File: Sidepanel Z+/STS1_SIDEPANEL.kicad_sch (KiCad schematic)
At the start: 3 parts, among them J1 Conn_02x04_Odd_Even, J2 Conn_02x02_Odd_Even

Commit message: Next fix
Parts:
- added J3: Conn_02x02_Odd_Even, STS_Connector:M808280442, symbol Connector_Generic:Conn_02x02_Odd_Even
- added TH1: Thermistor_NTC, Resistor_SMD:R_0805_2012Metric_Pad1.20x1.40mm_HandSolder, symbol Device:Thermistor_NTC
- Outline1: footprint USER_OUTLINE:OUTLINE_SidepanelY+ -> USER_OUTLINE:OUTLINE_SidepanelZ+
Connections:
- net GND: now also TH1.2
- net TEMP+: now also TH1.1
- new net AntennaDeployment/ANT_DEPLOY+: J3.1 (Pin_1), J3.2 (Pin_2)
- new net AntennaDeployment/ANT_DEPLOY-: J3.3 (Pin_3), J3.4 (Pin_4)
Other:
- added sheet AntennaDeployment (AntennaDeployment.kicad_sch)
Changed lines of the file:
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@@
 (kicad_sch (version 20211123) (generator eeschema)
   (paper "A4")
+  (junction (at 134.62 74.93) (diameter 0) (color 0 0 0 0)
+  )
+  (junction (at 134.62 72.39) (diameter 0) (color 0 0 0 0)
+  )
+  (wire (pts (xy 121.92 74.93) (xy 134.62 74.93))
+    (stroke (width 0) (type default) (color 0 0 0 0))
+  )
   (wire (pts (xy 26.67 67.31) (xy 34.29 67.31))
     (stroke (width 0) (type default) (color 0 0 0 0))
   )
+  (wire (pts (xy 138.43 39.37) (xy 152.4 39.37))
+    (stroke (width 0) (type default) (color 0 0 0 0))
+  )
   (wire (pts (xy 54.61 74.93) (xy 46.99 74.93))
     (stroke (width 0) (type default) (color 0 0 0 0))
@@
     (stroke (width 0) (type default) (color 0 0 0 0))
   )
+  (wire (pts (xy 134.62 35.56) (xy 152.4 35.56))
+    (stroke (width 0) (type default) (color 0 0 0 0))
+  )
   (wire (pts (xy 72.39 39.37) (xy 82.55 39.37))
     (stroke (width 0) (type default) (color 0 0 0 0))
@@
     (stroke (width 0) (type default) (color 0 0 0 0))
   )
+  (wire (pts (xy 30.48 93.345) (xy 30.48 97.155))
+    (stroke (width 0) (type default) (color 0 0 0 0))
+  )
+  (wire (pts (xy 138.43 74.93) (xy 138.43 39.37))
+    (stroke (width 0) (type default) (color 0 0 0 0))
+  )
+  (wire (pts (xy 134.62 74.93) (xy 138.43 74.93))
+    (stroke (width 0) (type default) (color 0 0 0 0))
+  )
   (wire (pts (xy 72.39 31.75) (xy 82.55 31.75))
     (stroke (width 0) (type default) (color 0 0 0 0))
@@
     (stroke (width 0) (type default) (color 0 0 0 0))
   )
+  (wire (pts (xy 134.62 72.39) (xy 134.62 35.56))
+    (stroke (width 0) (type default) (color 0 0 0 0))
+  )
   (wire (pts (xy 92.71 72.39) (xy 100.33 72.39))
     (stroke (width 0) (type default) (color 0 0 0 0))
   )
+  (wire (pts (xy 121.92 72.39) (xy 134.62 72.39))
+    (stroke (width 0) (type default) (color 0 0 0 0))
+  )
   (wire (pts (xy 72.39 41.91) (xy 82.55 41.91))
     (stroke (width 0) (type default) (color 0 0 0 0))
   )
+  (wire (pts (xy 30.48 104.775) (xy 30.48 107.95))
+    (stroke (width 0) (type default) (color 0 0 0 0))
+  )
   (wire (pts (xy 46.99 69.85) (xy 58.42 69.85))
     (stroke (width 0) (type default) (color 0 0 0 0))
@@
     (stroke (width 0) (type default) (color 0 0 0 0))
   )
+  (wire (pts (xy 30.48 93.345) (xy 37.465 93.345))
+    (stroke (width 0) (type default) (color 0 0 0 0))
+  )
   (wire (pts (xy 96.52 29.21) (xy 104.14 29.21))
     (stroke (width 0) (type default) (color 0 0 0 0))
@@
   )
   (label "SC1_V+" (at 82.55 29.21 180)
+    (effects (font (size 1.27 1.27)) (justify right bottom))
+  )
+  (label "TEMP+" (at 37.465 93.345 180)
     (effects (font (size 1.27 1.27)) (justify right bottom))
   )
@@
       (effects (font (size 1.27 1.27)) (justify left))
     )
-    (property "Footprint" "USER_OUTLINE:OUTLINE_SidepanelY+" (id 2) (at 22.86 22.86 0)
+    (property "Footprint" "USER_OUTLINE:OUTLINE_SidepanelZ+" (id 2) (at 22.86 22.86 0)
       (effects (font (size 1.27 1.27)) hide)
     )
@@
       (effects (font (size 1.27 1.27)) hide)
     )
+  )
+  (symbol (lib_id "power:GND") (at 30.48 107.95 0) (unit 1)
+    (in_bom yes) (on_board yes) (fields_autoplaced)
+    (property "Reference" "#PWR0113" (id 0) (at 30.48 114.3 0)
+      (effects (font (size 1.27 1.27)) hide)
+    )
+    (property "Value" "GND" (id 1) (at 30.48 113.03 0))
+    (property "Footprint" "" (id 2) (at 30.48 107.95 0)
+      (effects (font (size 1.27 1.27)) hide)
+    )
+    (property "Datasheet" "" (id 3) (at 30.48 107.95 0)
+      (effects (font (size 1.27 1.27)) hide)
+    )
+    (pin "1")
   )
   (symbol (lib_id "Connector_Generic:Conn_02x04_Odd_Even") (at 39.37 69.85 0) (unit 1)
@@
     (pin "4")
   )
+  (symbol (lib_id "Device:Thermistor_NTC") (at 30.48 100.965 0) (unit 1)
+    (in_bom yes) (on_board yes) (fields_autoplaced)
+    (property "Reference" "TH1" (id 0) (at 33.02 100.0124 0)
+      (effects (font (size 1.27 1.27)) (justify left))
+    )
+    (property "Value" "Thermistor_NTC" (id 1) (at 33.02 102.5524 0)
+      (effects (font (size 1.27 1.27)) (justify left))
+    )
+    (property "Footprint" "Resistor_SMD:R_0805_2012Metric_Pad1.20x1.40mm_HandSolder" (id 2) (at 30.48 99.695 0)
+      (effects (font (size 1.27 1.27)) hide)
+    )
+    (property "Datasheet" "~" (id 3) (at 30.48 99.695 0)
+      (effects (font (size 1.27 1.27)) hide)
+    )
+    (pin "1")
+    (pin "2")
+  )
+  (symbol (lib_id "Connector_Generic:Conn_02x02_Odd_Even") (at 127 72.39 0) (unit 1)
+    (in_bom yes) (on_board yes) (fields_autoplaced)
+    (property "Reference" "J3" (id 0) (at 128.27 67.4202 0))
+    (property "Value" "Conn_02x02_Odd_Even" (id 1) (at 128.27 69.9571 0))
+    (property "Footprint" "STS_Connector:M808280442" (id 2) (at 127 72.39 0)
+      (effects (font (size 1.27 1.27)) hide)
+    )
+    (property "Datasheet" "~" (id 3) (at 127 72.39 0)
+      (effects (font (size 1.27 1.27)) hide)
+    )
+    (pin "1")
+    (pin "2")
+    (pin "3")
+    (pin "4")
+  )
   (symbol (lib_id "power:GND") (at 101.6 76.2 0) (unit 1)
     (in_bom yes) (on_board yes) (fields_autoplaced)
@@
     )
     (pin "1")
+  )
+  (sheet (at 152.4 26.67) (size 21.59 15.24) (fields_autoplaced)
+    (stroke (width 0.1524) (type solid) (color 0 0 0 0))
+    (fill (color 0 0 0 0.0000))
+    (property "Sheet name" "AntennaDeployment" (id 0) (at 152.4 25.9584 0)
+      (effects (font (size 1.27 1.27)) (justify left bottom))
+    )
+    (property "Sheet file" "AntennaDeployment.kicad_sch" (id 1) (at 152.4 42.4946 0)
+      (effects (font (size 1.27 1.27)) (justify left top))
+    )
+    (pin "ANT_DEPLOY+" input (at 152.4 35.56 180)
+      (effects (font (size 1.27 1.27)) (justify left))
+    )
+    (pin "ANT_DEPLOY-" input (at 152.4 39.37 180)
+      (effects (font (size 1.27 1.27)) (justify left))
+    )
   )
   (sheet (at 50.8 26.67) (size 21.59 20.32) (fields_autoplaced)
@@
     (path "/9d03bb93-a9aa-424f-bd25-022f173efd1d" (page "3"))
     (path "/4f87559b-6bba-4ff6-97a7-dad9a308db2d" (page "4"))
+    (path "/13fd01c2-9c13-4b4c-bd8b-0bea989ca11e" (page "4"))
   )
   (symbol_instances
@@
       (reference "#PWR0112") (unit 1) (value "GND") (footprint "")
     )
+    (path "/7b859b76-0528-49b2-a54e-fd6560111b42"
+      (reference "#PWR0113") (unit 1) (value "GND") (footprint "")
+    )
     (path "/9d03bb93-a9aa-424f-bd25-022f173efd1d/744ba6a5-8f97-44b6-b33c-eda609bf7e9f"
       (reference "C1") (unit 1) (value "1u") (footprint "Capacitor_SMD:C_0603_1608Metric")
@@
     )
     (path "/4f87559b-6bba-4ff6-97a7-dad9a308db2d/65c76957-ccfc-4d5b-b7d9-2ee7c354f524"
-      (reference "DOUT2") (unit 1) (value "SMM4F5.0") (footprint "Diode_SMD:D_0603_1608Metric")
+      (reference "DOUT2") (unit 1) (value "SMM4F5.0") (footprint "LED_SMD:LED_0603_1608Metric")
     )
     (path "/9d03bb93-a9aa-424f-bd25-022f173efd1d/d9839939-8918-48f3-b4b2-d753b1d9a645"
@@
       (reference "J2") (unit 1) (value "Conn_02x02_Odd_Even") (footprint "STS_Connector:M808280442")
     )
+    (path "/bc26867e-2044-46bb-8920-dfb46ce37aad"
+      (reference "J3") (unit 1) (value "Conn_02x02_Odd_Even") (footprint "STS_Connector:M808280442")
+    )
     (path "/4f87559b-6bba-4ff6-97a7-dad9a308db2d/bfe4e68f-4cef-4b31-adff-8df094bc3870"
-      (reference "L_IN1") (unit 1) (value "10u") (footprint "Inductor_SMD:L_0603_1608Metric")
+      (reference "L_IN1") (unit 1) (value "10u") (footprint "Inductor_SMD:L_0805_2012Metric")
     )
     (path "/4f87559b-6bba-4ff6-97a7-dad9a308db2d/06a966cd-4913-436b-a217-7ac14ca6801e"
-      (reference "L_IN2") (unit 1) (value "10u") (footprint "Inductor_SMD:L_0603_1608Metric")
+      (reference "L_IN2") (unit 1) (value "10u") (footprint "Inductor_SMD:L_0805_2012Metric")
     )
     (path "/4f87559b-6bba-4ff6-97a7-dad9a308db2d/679b2e27-da22-4f13-a86e-25be83598a10"
@@
     )
     (path "/6503b427-07c6-4391-8fa6-4757fb4daa6c"
-      (reference "Outline1") (unit 1) (value "OUTLINE_Sidepanel") (footprint "USER_OUTLINE:OUTLINE_SidepanelY+")
+      (reference "Outline1") (unit 1) (value "OUTLINE_Sidepanel") (footprint "USER_OUTLINE:OUTLINE_SidepanelZ+")
     )
     (path "/4f87559b-6bba-4ff6-97a7-dad9a308db2d/548d9577-1c12-4167-8fdd-bb768e95bfba"
@@
       (reference "R32") (unit 1) (value "1k") (footprint "Resistor_SMD:R_0603_1608Metric")
     )
+    (path "/13fd01c2-9c13-4b4c-bd8b-0bea989ca11e/8b937a4c-4702-470b-b385-859583bbe895"
+      (reference "RD1") (unit 1) (value "22R") (footprint "Resistor_SMD:R_MiniMELF_MMA-0204")
+    )
+    (path "/13fd01c2-9c13-4b4c-bd8b-0bea989ca11e/39b2087d-31c5-4e79-b509-b7cd3aa9eab3"
+      (reference "RD2") (unit 1) (value "22R") (footprint "Resistor_SMD:R_MiniMELF_MMA-0204")
+    )
+    (path "/13fd01c2-9c13-4b4c-bd8b-0bea989ca11e/659cfc62-d3bc-492d-b2a4-d4a4d8ebb89d"
+      (reference "RD3") (unit 1) (value "22R") (footprint "Resistor_SMD:R_MiniMELF_MMA-0204")
+    )
     (path "/4f87559b-6bba-4ff6-97a7-dad9a308db2d/6f4b8cc8-d074-419d-84da-024a34781ce5"
       (reference "RF11") (unit 1) (value "1k") (footprint "Resistor_SMD:R_0603_1608Metric")
@@
     )
     (path "/4f87559b-6bba-4ff6-97a7-dad9a308db2d/e7b54c2f-482e-4a97-841f-62a80e0193a8"
-      (reference "SC1") (unit 1) (value "Solar_Cell") (footprint "STS_Connector:3G30A_40x80")
+      (reference "SC1") (unit 1) (value "Solar_Cell") (footprint "STS_Solarcells:3G30A_40x80")
     )
     (path "/4f87559b-6bba-4ff6-97a7-dad9a308db2d/3ad17c33-30d5-4097-824f-a9c26e6ca325"
-      (reference "SC2") (unit 1) (value "Solar_Cell") (footprint "STS_Connector:3G30A_40x80")
+      (reference "SC2") (unit 1) (value "Solar_Cell") (footprint "STS_Solarcells:3G30A_40x80")
+    )
+    (path "/a4d49e7c-3f1b-4d80-bed7-772a82216d80"
+      (reference "TH1") (unit 1) (value "Thermistor_NTC") (footprint "Resistor_SMD:R_0805_2012Metric_Pad1.20x1.40mm_HandSolder")
     )
     (path "/9d03bb93-a9aa-424f-bd25-022f173efd1d/a83d6342-0e16-4131-8bb9-e65e4d72dab0"

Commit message: release_2.0, Ordered PCBs
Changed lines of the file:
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@@
     )
     (path "/4f87559b-6bba-4ff6-97a7-dad9a308db2d/c6a198d2-e0e4-4d6d-8a2a-bdeb249501be"
-      (reference "DOUT1") (unit 1) (value "SMM4F5.0") (footprint "Diode_SMD:D_0603_1608Metric")
+      (reference "DOUT1") (unit 1) (value "SMM4F5.0") (footprint "SamacSys:STMITE")
     )
     (path "/4f87559b-6bba-4ff6-97a7-dad9a308db2d/65c76957-ccfc-4d5b-b7d9-2ee7c354f524"
-      (reference "DOUT2") (unit 1) (value "SMM4F5.0") (footprint "LED_SMD:LED_0603_1608Metric")
+      (reference "DOUT2") (unit 1) (value "SMM4F5.0") (footprint "SamacSys:STMITE")
     )
     (path "/9d03bb93-a9aa-424f-bd25-022f173efd1d/d9839939-8918-48f3-b4b2-d753b1d9a645"
@@
     )
     (path "/4f87559b-6bba-4ff6-97a7-dad9a308db2d/bfe4e68f-4cef-4b31-adff-8df094bc3870"
-      (reference "L_IN1") (unit 1) (value "10u") (footprint "Inductor_SMD:L_0805_2012Metric")
+      (reference "L_IN1") (unit 1) (value "10u") (footprint "STS_Inductor_SMD:XAL6060103MEC")
     )
     (path "/4f87559b-6bba-4ff6-97a7-dad9a308db2d/06a966cd-4913-436b-a217-7ac14ca6801e"
-      (reference "L_IN2") (unit 1) (value "10u") (footprint "Inductor_SMD:L_0805_2012Metric")
+      (reference "L_IN2") (unit 1) (value "10u") (footprint "STS_Inductor_SMD:XAL6060103MEC")
     )
     (path "/4f87559b-6bba-4ff6-97a7-dad9a308db2d/679b2e27-da22-4f13-a86e-25be83598a10"

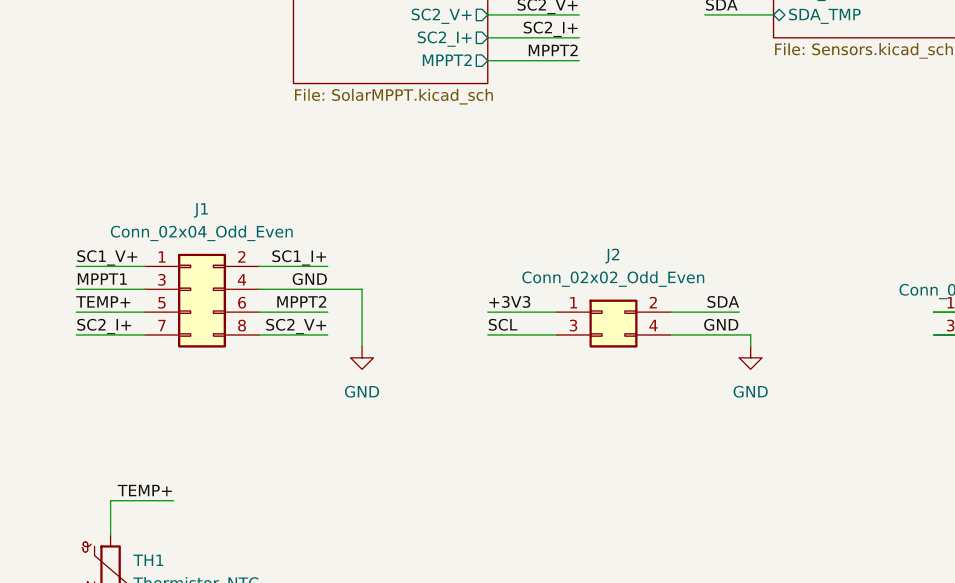
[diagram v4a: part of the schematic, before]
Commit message: changes to the solar cells footprint, added camera mounts
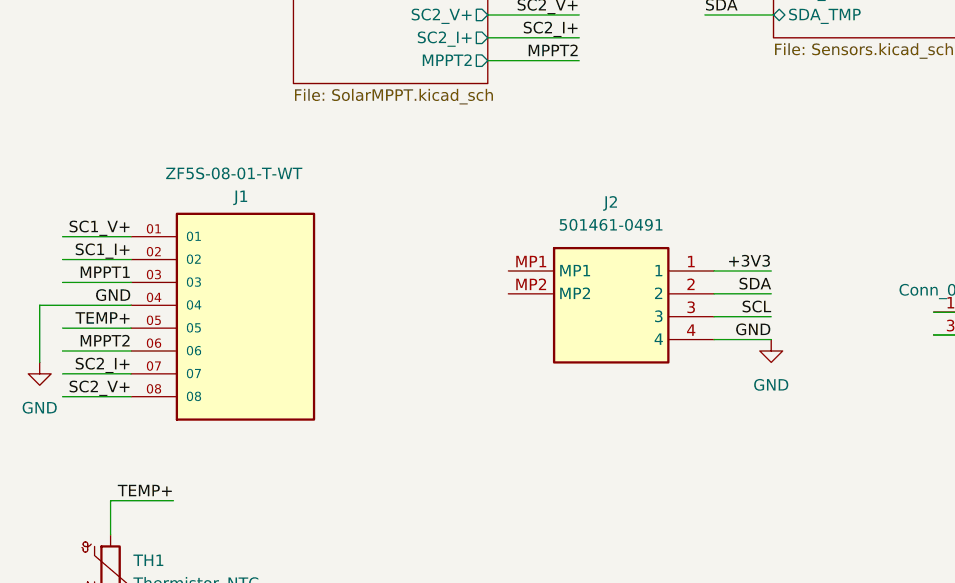
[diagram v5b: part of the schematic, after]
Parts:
- removed J1: Conn_02x04_Odd_Even, STS_Connector:M808280842, symbol Connector_Generic:Conn_02x04_Odd_Even
- removed J2: Conn_02x02_Odd_Even, STS_Connector:M808280442, symbol Connector_Generic:Conn_02x02_Odd_Even
- added J1: ZF5S-08-01-T-WT, STS_connector:SAMTEC_ZF5S-08-01-T-WT, symbol EPS connector:ZF5S-08-01-T-WT
- added UV1: 501461-0491, STS_connector:5014610491, symbol Connector:501461-0491
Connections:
- net +3V3: now also UV1.1
- net GND: now also J1.04, UV1.4
- net MPPT1: now also J1.03
- net MPPT2: now also J1.06
- net SC1_I+: now also J1.02
- net SC1_V+: now also J1.01
- net SC2_I+: now also J1.07
- net SC2_V+: now also J1.08
- net SCL: now also UV1.3
- net SDA: now also UV1.2
- net TEMP+: now also J1.05

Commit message: small adjustments
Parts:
- removed J1: ZF5S-08-01-T-WT, STS_connector:SAMTEC_ZF5S-08-01-T-WT, symbol EPS connector:ZF5S-08-01-T-WT
- added J1: Conn_01x08, STS_connector:SAMTEC_ZF5S-08-01-T-WT, symbol Connector_Generic:Conn_01x08
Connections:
- net GND: now also J1.04 (Pin_4)
- net MPPT1: now also J1.03 (Pin_3)
- net MPPT2: now also J1.06 (Pin_6)
- net SC1_I+: now also J1.02 (Pin_2)
- net SC1_V+: now also J1.01 (Pin_1)
- net SC2_I+: now also J1.07 (Pin_7)
- net SC2_V+: now also J1.08 (Pin_8)
- net TEMP+: now also J1.05 (Pin_5)

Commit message: added the libraries for the specific components
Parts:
- J1: footprint STS_connector:SAMTEC_ZF5S-08-01-T-WT -> STS_Connector:SAMTEC_ZF5S-08-01-T-WT
- UV1: footprint STS_connector:5014610491 -> STS_Connector:5014610491
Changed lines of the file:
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@@
       (effects (font (size 1.27 1.27)) (justify left))
     )
-    (property "Footprint" "STS_connector:SAMTEC_ZF5S-08-01-T-WT" (id 2) (at 37.592 71.628 0)
+    (property "Footprint" "STS_Connector:SAMTEC_ZF5S-08-01-T-WT" (id 2) (at 37.592 71.628 0)
       (effects (font (size 1.27 1.27)) hide)
     )
@@
       (effects (font (size 1.27 1.27)) hide)
     )
-    (property "Footprint" "STS_connector:5014610491" (id 2) (at 74.676 67.818 0)
+    (property "Footprint" "STS_Connector:5014610491" (id 2) (at 74.676 67.818 0)
       (effects (font (size 1.27 1.27)) hide)
     )
@@
     )
     (path "/66ace560-faee-4113-8a08-bf0ffa08a131"
-      (reference "J1") (unit 1) (value "Conn_01x08") (footprint "STS_connector:SAMTEC_ZF5S-08-01-T-WT")
+      (reference "J1") (unit 1) (value "Conn_01x08") (footprint "STS_Connector:SAMTEC_ZF5S-08-01-T-WT")
     )
     (path "/bc26867e-2044-46bb-8920-dfb46ce37aad"
@@
     )
     (path "/4f87559b-6bba-4ff6-97a7-dad9a308db2d/e7b54c2f-482e-4a97-841f-62a80e0193a8"
-      (reference "SC1") (unit 1) (value "Solar_Cell") (footprint "STS_Solarcells:3G30A_40x80")
+      (reference "SC1") (unit 1) (value "Solar_Cell") (footprint "STS_solder:3G30A_40x80_Z_SC1")
     )
     (path "/4f87559b-6bba-4ff6-97a7-dad9a308db2d/3ad17c33-30d5-4097-824f-a9c26e6ca325"
-      (reference "SC2") (unit 1) (value "Solar_Cell") (footprint "STS_Solarcells:3G30A_40x80")
+      (reference "SC2") (unit 1) (value "Solar_Cell") (footprint "STS_solder:3G30A_40x80_Z_SC2")
     )
     (path "/a4d49e7c-3f1b-4d80-bed7-772a82216d80"
@@
     )
     (path "/8b2997aa-f1dd-4a44-b565-4b1ba55f7b74"
-      (reference "UV1") (unit 1) (value "501461-0491") (footprint "STS_connector:5014610491")
-    )
-  )
+      (reference "UV1") (unit 1) (value "501461-0491") (footprint "STS_Connector:5014610491")
+    )
+  )
